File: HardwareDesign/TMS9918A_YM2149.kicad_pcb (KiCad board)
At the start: 2 copper layers, 150 x 90 mm, 46 parts, among them J001 Conn_02x40_Odd_Even, J701 RCJ-044, J702 Conn_01x02, J801 Conn_01x02, J802 Conn_02x09_Odd_Even, J803 SJ1-3525N, Q701 2N4401, U701 TMS9918A, U702 74HCT04, U703 74HCT32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

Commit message: more arranging of components
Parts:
- moved R803 102.4 mm to (232.5, 39.9)
- moved R804 102.4 mm to (221.7, 39.9)
- moved R807 102.4 mm to (221.7, 43.9)
- moved U801 84.8 mm to (166.6, 157.0), turned to -90 degrees
- moved U702 74.2 mm to (73.9, 85.8), turned to 90 degrees
- moved C704 69.1 mm to (167.9, 24.9)
- moved C703 69.1 mm to (162.2, 31.2)
- moved C705 69.1 mm to (162.2, 27.5)
- moved C707 69.1 mm to (158.7, 23.9)
- moved C706 69.1 mm to (173.5, 24.9)
- moved C701 67.9 mm to (87.1, 112.8)
- moved U703 62.1 mm to (145.0, 132.6), turned to 180 degrees
- moved R701 61.9 mm to (86.6, 99.6), turned to -90 degrees
- moved U704 57.4 mm to (145.0, 108.7), turned to 180 degrees
- moved C702 56.9 mm to (67.8, 77.7), turned to -90 degrees
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
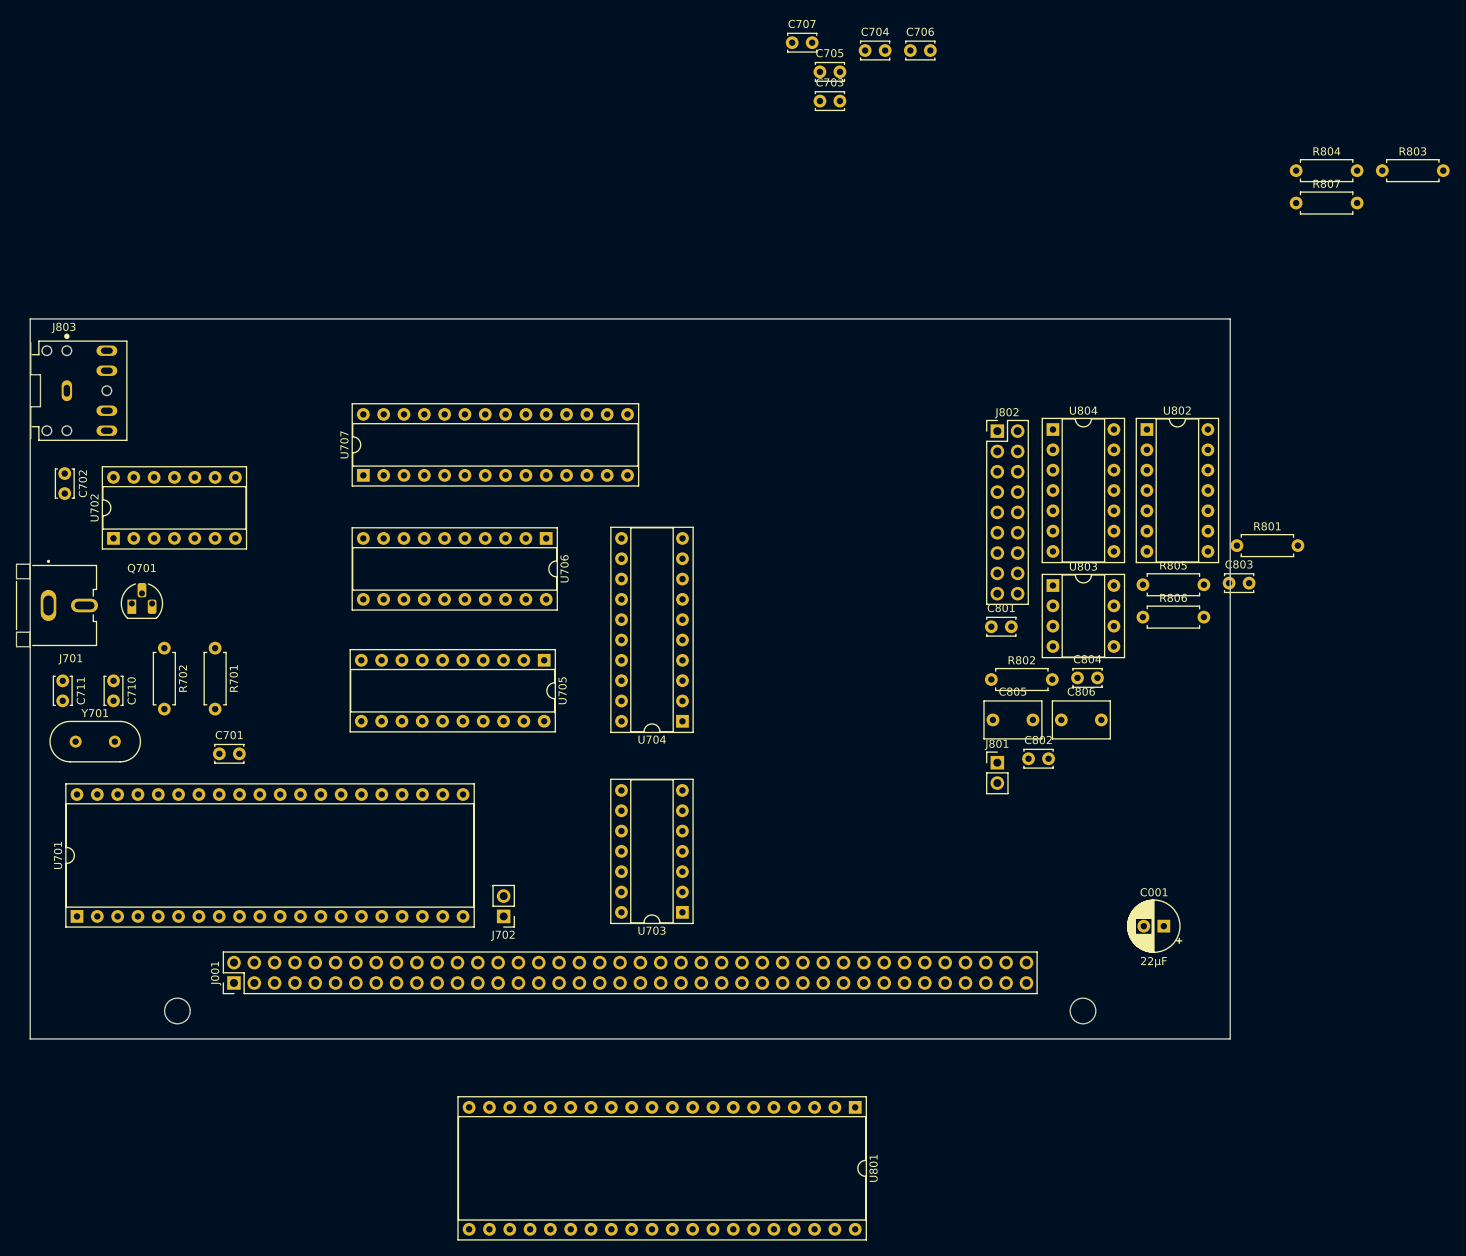
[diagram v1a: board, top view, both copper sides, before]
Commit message: better component layout
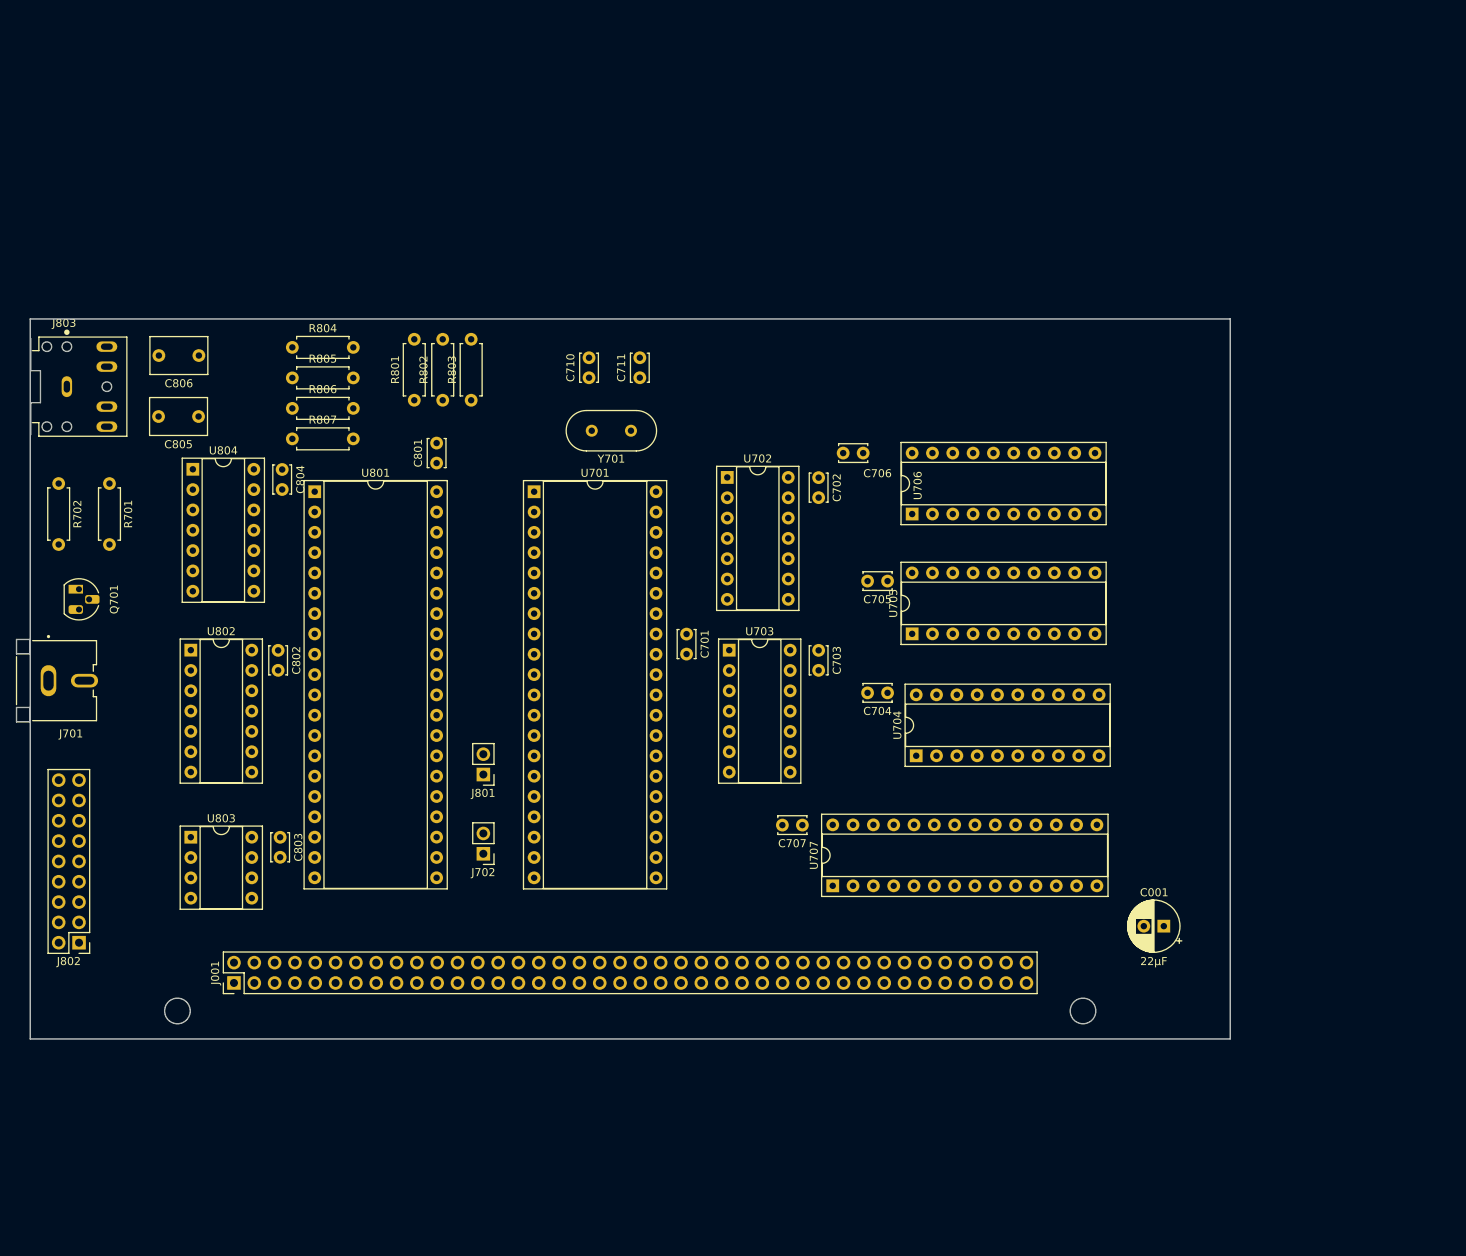
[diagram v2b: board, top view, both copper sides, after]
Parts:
- moved J802 131.4 mm to (69.6, 136.4), turned to 180 degrees
- moved R807 128.9 mm to (96.3, 73.4)
- moved R804 127.4 mm to (96.3, 62.0)
- moved C803 122.8 mm to (94.7, 123.2), turned to -90 degrees
- moved U802 122.7 mm to (83.6, 99.8)
- moved R803 117.5 mm to (118.6, 68.6), turned to 90 degrees
- moved C806 117.0 mm to (84.6, 63.0), turned to 180 degrees
- moved U803 112.3 mm to (83.6, 123.2)
- moved R806 109.5 mm to (96.3, 69.6)
- moved R805 109.4 mm to (96.3, 65.8)
- moved U804 107.6 mm to (83.8, 77.2)
- moved C805 106.3 mm to (84.5, 70.6), turned to 180 degrees
- moved R801 104.4 mm to (111.5, 68.6), turned to 90 degrees
- moved C804 102.8 mm to (95.0, 77.2), turned to -90 degrees
- moved U801 102.4 mm to (99.1, 80.0), turned to 0 degrees
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
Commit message: updated
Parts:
- moved Q701 1.37 mm to (70.1, 90.9)
- moved C805 0.76 mm to (85.3, 70.6)
- moved C806 0.76 mm to (85.3, 63.0)
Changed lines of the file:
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@@
 (kicad_pcb (version 20211014) (generator pcbnew)
   (general
-    (thickness 1.6002)
+    (thickness 1.6)
   )
   (paper "USLetter")
@@
   )
   (setup
+    (stackup
+      (layer "F.SilkS" (type "Top Silk Screen"))
+      (layer "F.Paste" (type "Top Solder Paste"))
+      (layer "F.Mask" (type "Top Solder Mask") (thickness 0.01))
+      (layer "F.Cu" (type "copper") (thickness 0.035))
+      (layer "dielectric 1" (type "core") (thickness 1.51) (material "FR4") (epsilon_r 4.5) (loss_tangent 0.02))
+      (layer "B.Cu" (type "copper") (thickness 0.035))
+      (layer "B.Mask" (type "Bottom Solder Mask") (thickness 0.01))
+      (layer "B.Paste" (type "Bottom Solder Paste"))
+      (layer "B.SilkS" (type "Bottom Silk Screen"))
+      (copper_finish "None")
+      (dielectric_constraints no)
+    )
     (pad_to_mask_clearance 0)
     (pcbplotparams
@@
   )
   (footprint "Package_TO_SOT_THT:TO-92_HandSolder" (layer "F.Cu")
-    (at 69.596 92.202 -90)
+    (at 70.104 90.932 -90)
     (descr "TO-92 leads molded, narrow, drill 0.75mm, handsoldering variant with enlarged pads (see NXP sot054_po.pdf)")
     (tags "to-92 sc-43 sc-43a sot54 PA33 transistor")
@@
       (effects (font (size 1 1) (thickness 0.15)))
     )
-    (fp_text value "2N4401" (at 1.27 2.79 90) (layer "F.Fab")
+    (fp_text value "2N4401" (at 1.27 3.302 90) (layer "F.SilkS")
       (effects (font (size 1 1) (thickness 0.15)))
     )
@@
     (property "Sheetname" "YM2149_Sound")
     (attr through_hole)
-    (fp_text reference "R802" (at 3.81 -2.37 90) (layer "F.SilkS")
-      (effects (font (size 1 1) (thickness 0.15)))
-    )
-    (fp_text value "3k" (at 3.81 2.37 90) (layer "F.Fab")
+    (fp_text reference "R802" (at 3.81 0 90) (layer "F.SilkS")
+      (effects (font (size 1 1) (thickness 0.15)))
+    )
+    (fp_text value "3k" (at -2.286 0 180) (layer "F.SilkS")
       (effects (font (size 1 1) (thickness 0.15)))
     )
@@
     (property "Sheetname" "YM2149_Sound")
     (attr through_hole)
-    (fp_text reference "R805" (at 3.81 -2.37) (layer "F.SilkS")
-      (effects (font (size 1 1) (thickness 0.15)))
-    )
-    (fp_text value "1k" (at 3.81 2.37) (layer "F.Fab")
+    (fp_text reference "R805" (at 3.81 0) (layer "F.SilkS")
+      (effects (font (size 1 1) (thickness 0.15)))
+    )
+    (fp_text value "1k" (at -2.286 0 90) (layer "F.SilkS")
       (effects (font (size 1 1) (thickness 0.15)))
     )
@@
       (effects (font (size 1 1) (thickness 0.15)))
     )
-    (fp_text value "22 pF" (at 1.25 2.3 90) (layer "F.Fab")
+    (fp_text value "22 pF" (at 4.806 -0.762 180) (layer "F.SilkS")
       (effects (font (size 1 1) (thickness 0.15)))
     )
@@
   )
   (footprint "Capacitor_THT:C_Rect_L7.0mm_W4.5mm_P5.00mm" (layer "F.Cu")
-    (at 84.582 62.992 180)
+    (at 85.344 62.992 180)
     (descr "C, Rect series, Radial, pin pitch=5.00mm, , length*width=7*4.5mm^2, Capacitor")
     (tags "C Rect series Radial pin pitch 5.00mm  length 7mm width 4.5mm Capacitor")
@@
     (property "Sheetname" "YM2149_Sound")
     (attr through_hole)
-    (fp_text reference "C806" (at 2.5 -3.5) (layer "F.SilkS")
-      (effects (font (size 1 1) (thickness 0.15)))
-    )
-    (fp_text value "2.2 uF" (at 2.5 3.5) (layer "F.Fab")
+    (fp_text reference "C806" (at 7.874 0 90) (layer "F.SilkS")
+      (effects (font (size 1 1) (thickness 0.15)))
+    )
+    (fp_text value "2.2 uF" (at -2.794 0 90) (layer "F.Fab")
       (effects (font (size 1 1) (thickness 0.15)))
     )
@@
     (property "Sheetname" "YM2149_Sound")
     (attr through_hole)
-    (fp_text reference "R807" (at 3.81 -2.37) (layer "F.SilkS")
-      (effects (font (size 1 1) (thickness 0.15)))
-    )
-    (fp_text value "1k" (at 3.81 2.37) (layer "F.Fab")
+    (fp_text reference "R807" (at 3.81 0) (layer "F.SilkS")
+      (effects (font (size 1 1) (thickness 0.15)))
+    )
+    (fp_text value "1k" (at -2.286 0 90) (layer "F.SilkS")
       (effects (font (size 1 1) (thickness 0.15)))
     )
@@
     (property "Sheetname" "YM2149_Sound")
     (attr through_hole)
-    (fp_text reference "R803" (at 3.81 -2.37 90) (layer "F.SilkS")
-      (effects (font (size 1 1) (thickness 0.15)))
-    )
-    (fp_text value "3k" (at 3.81 2.37 90) (layer "F.Fab")
+    (fp_text reference "R803" (at 3.81 0 90) (layer "F.SilkS")
+      (effects (font (size 1 1) (thickness 0.15)))
+    )
+    (fp_text value "3k" (at -2.286 0 180) (layer "F.SilkS")
       (effects (font (size 1 1) (thickness 0.15)))
     )
@@
     (property "Sheetname" "TMS9918ADisplay")
     (attr through_hole)
-    (fp_text reference "Y701" (at 2.45 -3.525) (layer "F.SilkS")
-      (effects (font (size 1 1) (thickness 0.15)))
-    )
-    (fp_text value "10.738635 MHz" (at 2.45 3.525) (layer "F.Fab")
+    (fp_text reference "Y701" (at 9.562 0.254 90) (layer "F.SilkS")
+      (effects (font (size 1 1) (thickness 0.15)))
+    )
+    (fp_text value "10.738635 MHz" (at 2.45 3.525) (layer "F.SilkS")
       (effects (font (size 1 1) (thickness 0.15)))
     )
@@
     (property "Sheetname" "YM2149_Sound")
     (attr through_hole)
-    (fp_text reference "R804" (at 3.81 -2.37) (layer "F.SilkS")
-      (effects (font (size 1 1) (thickness 0.15)))
-    )
-    (fp_text value "1k" (at 3.81 2.37) (layer "F.Fab")
+    (fp_text reference "R804" (at 3.81 0) (layer "F.SilkS")
+      (effects (font (size 1 1) (thickness 0.15)))
+    )
+    (fp_text value "1k" (at -2.286 0 90) (layer "F.SilkS")
       (effects (font (size 1 1) (thickness 0.15)))
     )
@@
       (effects (font (size 1 1) (thickness 0.15)))
     )
-    (fp_text value "YM2149" (at 7.62 -4.572) (layer "F.Fab")
+    (fp_text value "YM2149" (at 7.366 51.816) (layer "F.SilkS")
       (effects (font (size 1 1) (thickness 0.15)))
     )
@@
     (property "Sheetname" "YM2149_Sound")
     (attr through_hole)
-    (fp_text reference "R806" (at 3.81 -2.37) (layer "F.SilkS")
-      (effects (font (size 1 1) (thickness 0.15)))
-    )
-    (fp_text value "1k" (at 3.81 2.37) (layer "F.Fab")
+    (fp_text reference "R806" (at 3.81 0) (layer "F.SilkS")
+      (effects (font (size 1 1) (thickness 0.15)))
+    )
+    (fp_text value "1k" (at -2.286 0 90) (layer "F.SilkS")
       (effects (font (size 1 1) (thickness 0.15)))
     )
@@
     (property "Sheetname" "YM2149_Sound")
     (attr through_hole)
-    (fp_text reference "R801" (at 3.81 -2.37 90) (layer "F.SilkS")
-      (effects (font (size 1 1) (thickness 0.15)))
-    )
-    (fp_text value "3k" (at 3.81 2.37 90) (layer "F.Fab")
+    (fp_text reference "R801" (at 3.81 0 90) (layer "F.SilkS")
+      (effects (font (size 1 1) (thickness 0.15)))
+    )
+    (fp_text value "3k" (at -2.286 0 180) (layer "F.SilkS")
       (effects (font (size 1 1) (thickness 0.15)))
     )
@@
   )
   (footprint "Capacitor_THT:C_Rect_L7.0mm_W4.5mm_P5.00mm" (layer "F.Cu")
-    (at 84.542 70.612 180)
+    (at 85.304 70.612 180)
     (descr "C, Rect series, Radial, pin pitch=5.00mm, , length*width=7*4.5mm^2, Capacitor")
     (tags "C Rect series Radial pin pitch 5.00mm  length 7mm width 4.5mm Capacitor")
@@
     (property "Sheetname" "YM2149_Sound")
     (attr through_hole)
-    (fp_text reference "C805" (at 2.5 -3.5) (layer "F.SilkS")
-      (effects (font (size 1 1) (thickness 0.15)))
-    )
-    (fp_text value "2.2 uF" (at 2.5 3.5) (layer "F.Fab")
+    (fp_text reference "C805" (at 7.834 0 90) (layer "F.SilkS")
+      (effects (font (size 1 1) (thickness 0.15)))
+    )
+    (fp_text value "2.2 uF" (at -2.834 0 90) (layer "F.Fab")
       (effects (font (size 1 1) (thickness 0.15)))
     )
@@
       (effects (font (size 1 1) (thickness 0.15)))
     )
-    (fp_text value "100 nF" (at 1.25 2.3 90) (layer "F.Fab")
+    (fp_text value "100 nF" (at 1.25 2.3 90) (layer "F.SilkS")
       (effects (font (size 1 1) (thickness 0.15)))
     )
@@
       (effects (font (size 1 1) (thickness 0.15)))
     )
-    (fp_text value "22 pF" (at 1.25 2.3 90) (layer "F.Fab")
+    (fp_text value "22 pF" (at 4.806 -0.762 180) (layer "F.SilkS")
       (effects (font (size 1 1) (thickness 0.15)))
     )
@@
       (effects (font (size 1 1) (thickness 0.15)))
     )
-    (fp_text value "TMS9918A" (at 7.62 50.59) (layer "F.Fab")
-      (effects (font (size 1 1) (thickness 0.15)))
-    )
+    (fp_text value "TMS9918A" (at 7.879 51.811) (layer "F.SilkS")
+      (effects (font (size 1 1) (thickness 0.15)))
+    )

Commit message: started to route tracks
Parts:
- moved C710 11.9 mm to (145.3, 65.8), turned to -90 degrees
- moved Y701 1.91 mm to (140.2, 73.4), turned to 0 degrees
- moved C711 0.51 mm to (140.2, 65.8), turned to -90 degrees
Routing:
- net /A0: track 0.00 -> 113.0 mm, vias 0 -> 2
- net /D0: track 0.00 -> 105.8 mm, vias 0 -> 2
- net /D1: track 0.00 -> 97.9 mm, vias 0 -> 2
- net Net-(Q701-Pad2): track 0.00 -> 93.7 mm, vias 0 -> 1
- net /D2: track 0.00 -> 93.5 mm, vias 0 -> 2
- net /D3: track 0.00 -> 83.5 mm, vias 0 -> 2
- net /D4: track 0.00 -> 53.6 mm, vias 0 -> 1
- net /D5: track 0.00 -> 48.7 mm, vias 0 -> 1
- net /D6: track 0.00 -> 43.7 mm, vias 0 -> 1
- net /D7: track 0.00 -> 38.4 mm, vias 0 -> 1
- net /~{IRQ2}: track 0.00 -> 16.8 mm
- net Net-(C710-Pad2): track 0.00 -> 16.6 mm
- net Net-(J701-Pad2): track 0.00 -> 13.2 mm
- net Net-(C711-Pad2): track 0.00 -> 12.4 mm
- net /~{WMEM}: track 0.00 -> 7.62 mm
